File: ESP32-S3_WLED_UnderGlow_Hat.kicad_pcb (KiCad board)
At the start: 6 copper layers, 31 x 30 mm, 149 parts, among them CN301 SM32B-NSHDZS-1-TF, CN302 SM32B-NSHDZS-1-TF, Q901 NTLJS17D0P03P8Z, U701 TCAN4550-Q1, U702 74LV1T125, U801 74LV1T125, U802 74LV1T125, U803 74LV1T125, U804 74LV1T125, U805 74LV1T125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

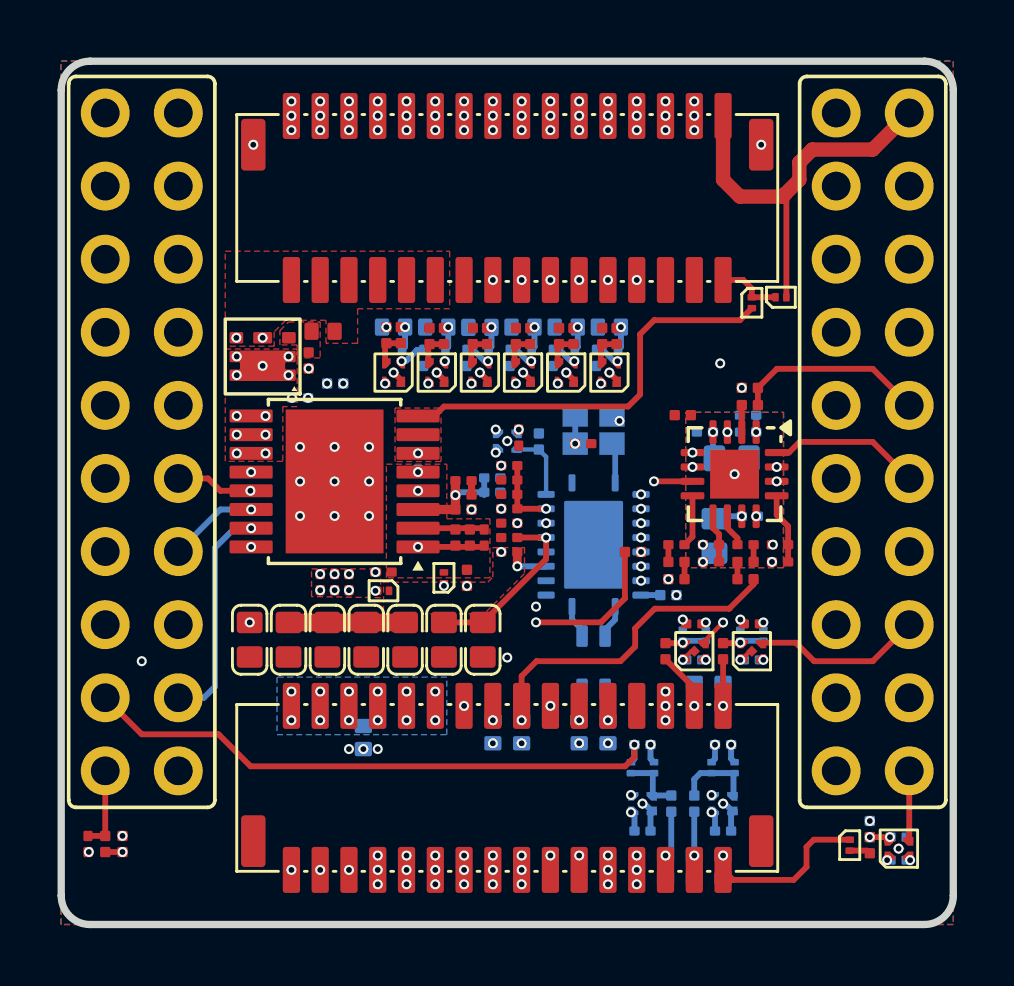
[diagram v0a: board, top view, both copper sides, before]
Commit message: Created new edge cut
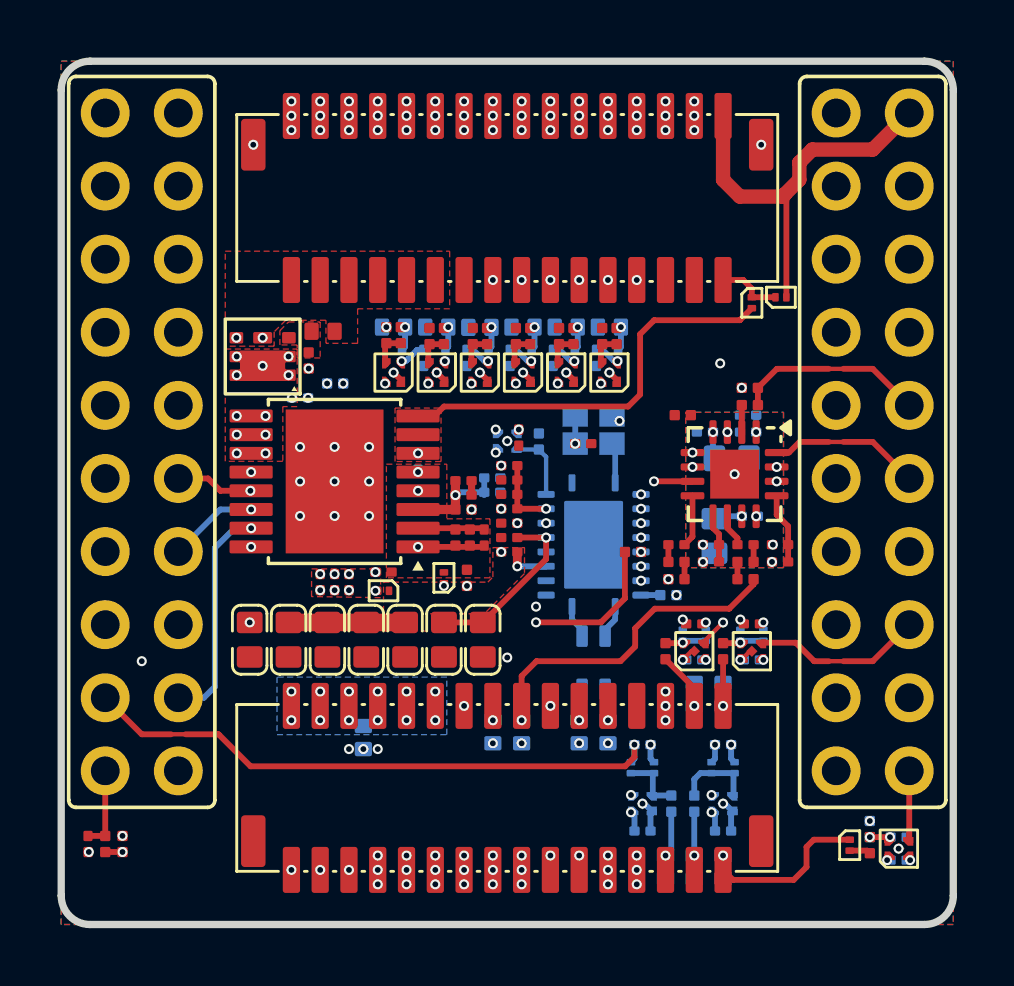
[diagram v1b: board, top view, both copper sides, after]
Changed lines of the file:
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@@
 			(layer "F.SilkS")
 		)
-		(fp_line
-			(start -15.5 -13.5)
-			(end -15.5 14.5)
-			(stroke
-				(width 0.254)
-				(type solid)
-			)
-			(layer "Edge.Cuts")
-		)
-		(fp_line
-			(start -14.5 -14.5)
-			(end 14.5 -14.5)
-			(stroke
-				(width 0.254)
-				(type solid)
-			)
-			(layer "Edge.Cuts")
-		)
-		(fp_line
-			(start -14.5 15.5)
-			(end 14.5 15.5)
-			(stroke
-				(width 0.254)
-				(type solid)
-			)
-			(layer "Edge.Cuts")
-		)
-		(fp_line
-			(start 15.5 -13.5)
-			(end 15.5 14.5)
-			(stroke
-				(width 0.254)
-				(type solid)
-			)
-			(layer "Edge.Cuts")
-		)
-		(fp_arc
-			(start -15.5 -13.5)
-			(mid -15.207107 -14.207107)
-			(end -14.5 -14.5)
-			(stroke
-				(width 0.254)
-				(type default)
-			)
-			(layer "Edge.Cuts")
-		)
-		(fp_arc
-			(start -14.5 15.5)
-			(mid -15.207107 15.207107)
-			(end -15.5 14.5)
-			(stroke
-				(width 0.254)
-				(type default)
-			)
-			(layer "Edge.Cuts")
-		)
-		(fp_arc
-			(start 14.5 -14.5)
-			(mid 15.207107 -14.207107)
-			(end 15.5 -13.5)
-			(stroke
-				(width 0.254)
-				(type default)
-			)
-			(layer "Edge.Cuts")
-		)
-		(fp_arc
-			(start 15.5 14.5)
-			(mid 15.207107 15.207107)
-			(end 14.5 15.5)
-			(stroke
-				(width 0.254)
-				(type default)
-			)
-			(layer "Edge.Cuts")
-		)
 		(fp_rect
 			(start -15.494 -14.224)
@@
 			(layer "B.Fab")
 		)
+		(fp_line
+			(start -15.5 -13.5)
+			(end -15.5 14.5)
+			(stroke
+				(width 0.254)
+				(type solid)
+			)
+			(layer "F.Fab")
+		)
+		(fp_line
+			(start -14.5 -14.5)
+			(end 14.5 -14.5)
+			(stroke
+				(width 0.254)
+				(type solid)
+			)
+			(layer "F.Fab")
+		)
+		(fp_line
+			(start -14.5 15.5)
+			(end 14.5 15.5)
+			(stroke
+				(width 0.254)
+				(type solid)
+			)
+			(layer "F.Fab")
+		)
+		(fp_line
+			(start 15.5 -13.5)
+			(end 15.5 14.5)
+			(stroke
+				(width 0.254)
+				(type solid)
+			)
+			(layer "F.Fab")
+		)
 		(fp_rect
 			(start -15.24 -13.97)
@@
 			(layer "F.Fab")
 		)
+		(fp_arc
+			(start -15.5 -13.5)
+			(mid -15.207107 -14.207107)
+			(end -14.5 -14.5)
+			(stroke
+				(width 0.254)
+				(type default)
+			)
+			(layer "F.Fab")
+		)
+		(fp_arc
+			(start -14.5 15.5)
+			(mid -15.207107 15.207107)
+			(end -15.5 14.5)
+			(stroke
+				(width 0.254)
+				(type default)
+			)
+			(layer "F.Fab")
+		)
+		(fp_arc
+			(start 14.5 -14.5)
+			(mid 15.207107 -14.207107)
+			(end 15.5 -13.5)
+			(stroke
+				(width 0.254)
+				(type default)
+			)
+			(layer "F.Fab")
+		)
+		(fp_arc
+			(start 15.5 14.5)
+			(mid 15.207107 15.207107)
+			(end 14.5 15.5)
+			(stroke
+				(width 0.254)
+				(type default)
+			)
+			(layer "F.Fab")
+		)
+		(fp_text user "<-- Suggested PCB outline"
+			(at 15.5 14 0)
+			(unlocked yes)
+			(layer "F.Fab")
+			(effects
+				(font
+					(size 1 1)
+					(thickness 0.1)
+				)
+				(justify left bottom)
+			)
+		)
 		(fp_text user "${REFERENCE}"
 			(at 0 2.5 0)
@@
 	)
 	(gr_line
+		(start 152.4 128.15)
+		(end 152.4 100.15)
+		(stroke
+			(width 0.254)
+			(type default)
+		)
+		(layer "Edge.Cuts")
+	)
+	(gr_arc
+		(start 152.4 100.15)
+		(mid 152.692893 99.442893)
+		(end 153.4 99.15)
+		(stroke
+			(width 0.254)
+			(type default)
+		)
+		(layer "Edge.Cuts")
+	)
+	(gr_line
+		(start 153.4 99.15)
+		(end 182.4 99.15)
+		(stroke
+			(width 0.254)
+			(type default)
+		)
+		(layer "Edge.Cuts")
+	)
+	(gr_line
+		(start 183.4 100.15)
+		(end 183.4 128.15)
+		(stroke
+			(width 0.254)
+			(type default)
+		)
+		(layer "Edge.Cuts")
+	)
+	(gr_line
+		(start 182.4 129.15)
+		(end 153.4 129.15)
+		(stroke
+			(width 0.254)
+			(type default)
+		)
+		(layer "Edge.Cuts")
+	)
+	(gr_arc
+		(start 182.4 99.15)
+		(mid 183.107107 99.442893)
+		(end 183.4 100.15)
+		(stroke
+			(width 0.254)
+			(type default)
+		)
+		(layer "Edge.Cuts")
+	)
+	(gr_arc
+		(start 183.4 128.15)
+		(mid 183.107107 128.857107)
+		(end 182.4 129.15)
+		(stroke
+			(width 0.254)
+			(type default)
+		)
+		(layer "Edge.Cuts")
+	)
+	(gr_arc
+		(start 153.4 129.15)
+		(mid 152.692893 128.857107)
+		(end 152.4 128.15)
+		(stroke
+			(width 0.254)
+			(type default)
+		)
+		(layer "Edge.Cuts")
+	)
+	(gr_line
 		(start 151.9 108.517)
 		(end 183.9 108.517)
@@
 	(segment
 		(start 155.2 122.54)
-		(end 157.867 122.54)
+		(end 156.216 122.54)
 		(width 0.2032)
 		(layer "F.Cu")
@@
 	)
 	(segment
+		(start 156.216 122.54)
+		(end 156.724 122.54)
+		(width 0.1524)
+		(layer "F.Cu")
+		(net 6)
+	)
+	(segment
+		(start 157.867 122.54)
+		(end 156.724 122.54)
+		(width 0.2032)
+		(layer "F.Cu")
+		(net 6)
+	)
+	(segment
 		(start 171.997 123.653)
 		(end 172.32 123.33)
@@
 	(segment
 		(start 180.6 120)
+		(end 179.584 120)
+		(width 0.2032)
+		(layer "F.Cu")
+		(net 62)
+	)
+	(segment
+		(start 179.076 120)
 		(end 178.568 120)
 		(width 0.2032)
@@
 	)
 	(segment
+		(start 179.076 120)
+		(end 179.584 120)
+		(width 0.1524)
+		(layer "F.Cu")
+		(net 62)
+	)
+	(segment
 		(start 174.76 119.358)
 		(end 174.76 119.293)
@@
 	)
 	(segment
+		(start 179.076 109.84)
+		(end 179.584 109.84)
+		(width 0.1524)
+		(layer "F.Cu")
+		(net 86)
+	)
+	(segment
 		(start 176.61 110.5)
 		(end 177.27 109.84)
@@
 	)
 	(segment
+		(start 180.6 109.84)
+		(end 179.584 109.84)
+		(width 0.2032)
+		(layer "F.Cu")
+		(net 86)
+	)
+	(segment
 		(start 177.27 109.84)
-		(end 180.6 109.84)
+		(end 179.076 109.84)
 		(width 0.2032)
 		(layer "F.Cu")
@@
 	)
 	(segment
+		(start 179.076 112.38)
+		(end 179.584 112.38)
+		(width 0.1524)
+		(layer "F.Cu")
+		(net 88)
+	)
+	(segment
 		(start 177.69 112.75)
 		(end 178.06 112.38)
@@
 	(segment
 		(start 178.06 112.38)
-		(end 180.6 112.38)
+		(end 179.076 112.38)
 		(width 0.2032)
 		(layer "F.Cu")
@@
 	)
 	(segment
+		(start 180.6 112.38)
+		(end 179.584 112.38)
+		(width 0.2032)
+		(layer "F.Cu")
+		(net 88)
+	)
+	(segment
 		(start 177.2625 112.75)
 		(end 177.69 112.75)
@@
 			(clearance 0.1)
 		)
-		(min_thickness 0.15)
+		(min_thickness 0.1)
 		(filled_areas_thickness no)
 		(fill yes

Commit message: JLCPCB: W2026061412450502 2026-06-14 PCB: Y62-5297522A PCBA: SMT026061460215-5297522A
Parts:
- D701, D801, D803, D804, D806, D807, D809, D810, D812, D813, D901, D902, D903, D904, D908, D909, D912, D913, D914: footprint Personal_FootprintLibrary:DSN0603-2 -> My Package_Leadless:DFN0603-2
- moved C706 0.85 mm to (167.9, 119.3)
- moved C704 0.65 mm to (166.3, 119.3)
- moved C710 0.45 mm to (164.8, 119.3)
- moved C701 0.35 mm to (158.6, 119.3)
- moved C709 0.25 mm to (163.2, 119.3)
- moved C707 0.15 mm to (160.2, 119.3)
- renumbered U201 to U301
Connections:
- net +V_{SUP} renamed /IO_Board/CAN Bus/+V_{SUP}
- net GNDA renamed /IO_Board/GR86 Inputs/GND3
- U301 pad 12: /IO_Board/IO00 -> unconnected-(U301A-IO00-Pad12)
- U301 pad 21: /IO_Board/IO46 -> unconnected-(U301B-IO46-Pad21)
- U301 pad 22: /IO_Board/IO45 -> unconnected-(U301B-IO45-Pad22)
- U301 pad 28: +5V_{EXT} -> unconnected-(U301B-+5V_{EXT}-Pad28)
- U301 pad 3: /IO_Board/IO01 -> unconnected-(U301A-IO01-Pad3)
- U301 pad 4: /IO_Board/IO03 -> unconnected-(U301A-IO03-Pad4)
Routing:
- net /IO_Board/CAN Bus/+V_{SUP}: track 5.55 -> 1.50 mm
- net /IO_Board/CAN Bus/V_{CC_{OUT}}: track 6.21 -> 4.51 mm
- net /IO_Board/LED1: track 22.0 -> 23.1 mm
- net +5V_{FUSED}: track 67.5 -> 68.4 mm
- net GND0: track 14.1 -> 13.4 mm
- net /IO_Board/Data3: track 4.25 -> 3.61 mm
- net /IO_Board/AUX_{R}: track 11.0 -> 10.4 mm
- net /IO_Board/Data2: track 4.70 -> 4.13 mm
- net /IO_Board/AUX_{L}: track 9.44 -> 9.08 mm, vias 2 -> 1
- net +V_{SW}: vias 2 -> 0
- net (no net): vias 1 -> 0
- added copper zone on F.Cu, net /IO_Board/CAN Bus/V_{CC_{OUT}}
- added copper zone on B.Cu, net /IO_Board/WLED Outputs/V_{OUT2}
- added copper zone on F.Cu, net GND0
- removed copper zone on In2.Cu, net +V_{SW}
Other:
- board text added: "JLCJLCJLCJLC"
- board text added: "RHK WLED I/O Hat © Robert Kean 2026"
